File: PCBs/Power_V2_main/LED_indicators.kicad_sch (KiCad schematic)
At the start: 3 parts, among them J1 Conn_01x04, Q2 RQ6E080AJ, Q3 RQ6E080AJ

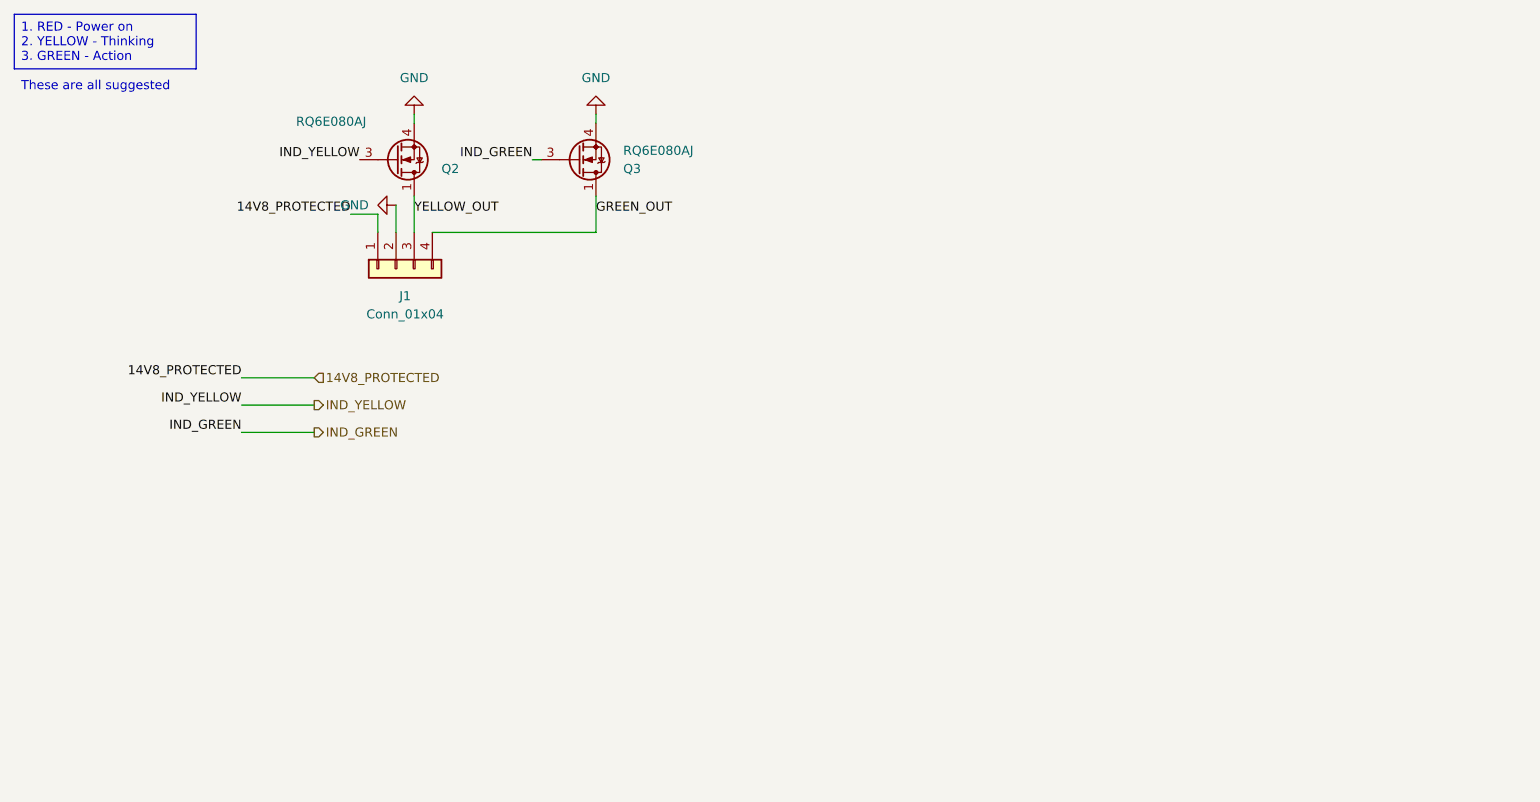
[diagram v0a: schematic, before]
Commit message: modification to LED switches
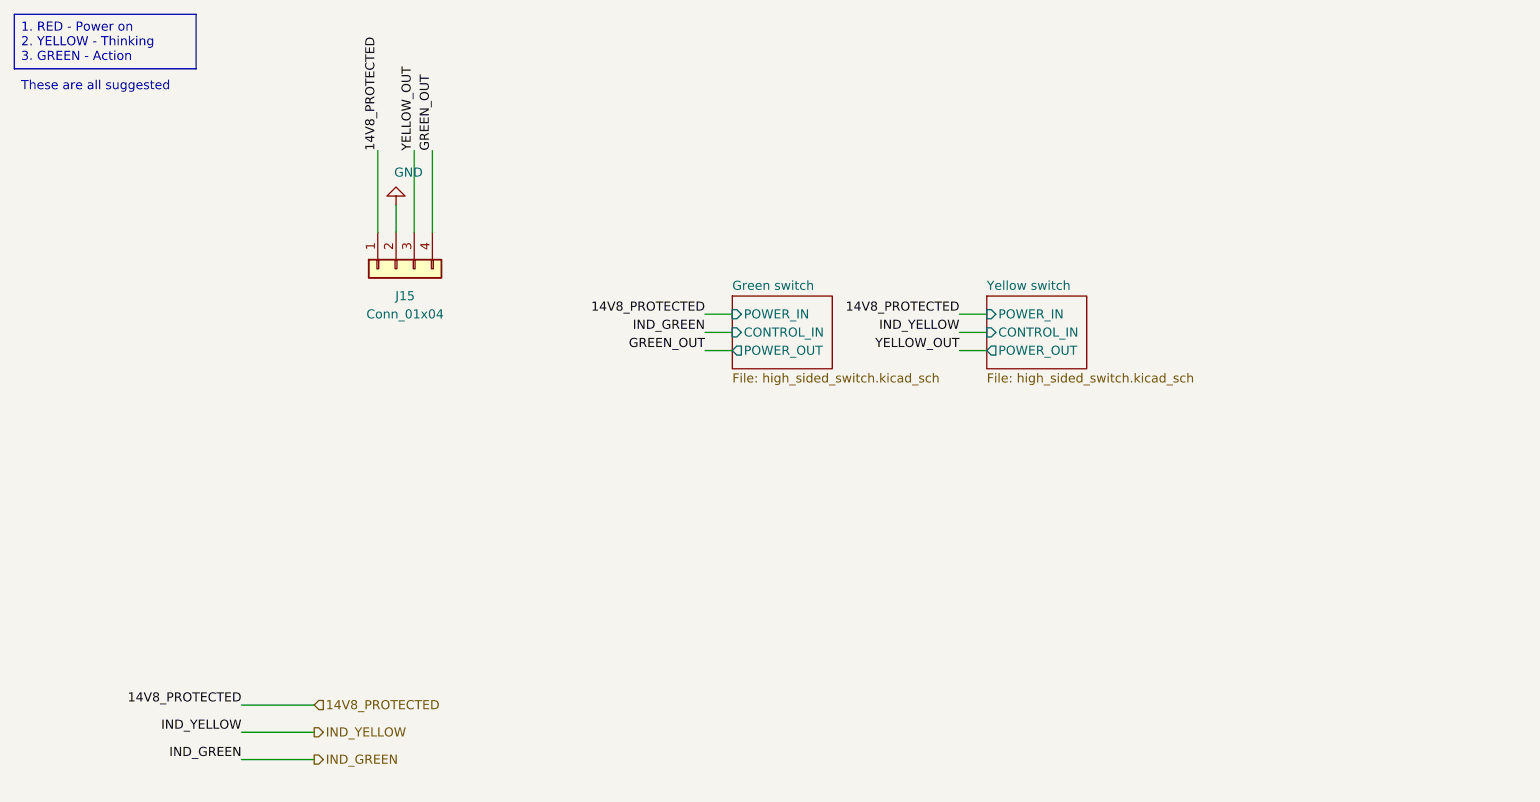
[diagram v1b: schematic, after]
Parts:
- removed J1: Conn_01x04, Connector_JST:JST_GH_BM04B-GHS-TBT_1x04-1MP_P1.25mm_Vertical, symbol Connector_Generic:Conn_01x04
- removed Q2, Q3: RQ6E080AJ, Package_TO_SOT_SMD:TSOT-23-6, symbol Transistor_FET:RQ6E080AJ
- added J15: Conn_01x04, Connector_JST:JST_GH_BM04B-GHS-TBT_1x04-1MP_P1.25mm_Vertical, symbol Connector_Generic:Conn_01x04
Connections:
- net 14V8_PROTECTED: now also J15.1 (Pin_1)
- net GND: now also J15.2 (Pin_2)
- net GREEN_OUT: now also J15.4 (Pin_4)
- net YELLOW_OUT: now also J15.3 (Pin_3)
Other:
- added sheet Green switch (high_sided_switch.kicad_sch)
- added sheet Yellow switch (high_sided_switch.kicad_sch)

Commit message: follow up changes from meeting
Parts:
- removed J15: Conn_01x04, Connector_JST:JST_GH_BM04B-GHS-TBT_1x04-1MP_P1.25mm_Vertical, symbol Connector_Generic:Conn_01x04
- added J1: Conn_01x05, Connector_JST:JST_EH_B5B-EH-A_1x05_P2.50mm_Vertical, symbol Connector_Generic:Conn_01x05
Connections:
- net 14V8_PROTECTED: now also J1.1 (Pin_1)
- net GND: now also J1.2 (Pin_2)
- net GREEN_OUT: now also J1.5 (Pin_5)
- net YELLOW_OUT: now also J1.4 (Pin_4)
- new net SIREN_OUT: J1.3 (Pin_3)
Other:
- added sheet Siren switch (high_sided_switch.kicad_sch)
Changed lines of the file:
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@@
 	(generator_version "9.0")
 	(paper "A4")
-	(text_box "1. RED - Power on\n2. YELLOW - Thinking\n3. GREEN - Action\n\nThese are all suggested"
+	(text_box "1. RED - Power on\n2. YELLOW - Thinking\n3. GREEN - Action\n4. SIREN  - All hell broken loose\n\nThese are all suggested"
 		(exclude_from_sim no)
 		(at 13.97 13.97 0)
-		(size 25.4 7.62)
+		(size 25.4 11.43)
 		(margins 0.9525 0.9525 0.9525 0.9525)
 		(stroke
@@
 	(wire
 		(pts
+			(xy 45.72 110.49) (xy 55.88 110.49)
+		)
+		(stroke
+			(width 0)
+			(type default)
+		)
+	)
+	(wire
+		(pts
+			(xy 181.61 55.88) (xy 185.42 55.88)
+		)
+		(stroke
+			(width 0)
+			(type default)
+		)
+	)
+	(wire
+		(pts
 			(xy 72.39 33.02) (xy 72.39 44.45)
 		)
@@
 	(wire
 		(pts
-			(xy 45.72 110.49) (xy 55.88 110.49)
-		)
-		(stroke
-			(width 0)
-			(type default)
-		)
-	)
-	(wire
-		(pts
 			(xy 64.77 33.02) (xy 64.77 44.45)
 		)
@@
 	(wire
 		(pts
+			(xy 181.61 60.96) (xy 185.42 60.96)
+		)
+		(stroke
+			(width 0)
+			(type default)
+		)
+	)
+	(wire
+		(pts
 			(xy 114.3 58.42) (xy 110.49 58.42)
 		)
@@
 	(wire
 		(pts
+			(xy 45.72 120.65) (xy 55.88 120.65)
+		)
+		(stroke
+			(width 0)
+			(type default)
+		)
+	)
+	(wire
+		(pts
 			(xy 110.49 60.96) (xy 114.3 60.96)
 		)
@@
 	(wire
 		(pts
+			(xy 74.93 33.02) (xy 74.93 44.45)
+		)
+		(stroke
+			(width 0)
+			(type default)
+		)
+	)
+	(wire
+		(pts
+			(xy 181.61 58.42) (xy 185.42 58.42)
+		)
+		(stroke
+			(width 0)
+			(type default)
+		)
+	)
+	(wire
+		(pts
 			(xy 69.85 33.02) (xy 69.85 44.45)
 		)
@@
 			(width 0)
 			(type default)
+		)
+	)
+	(label "IND_SIREN"
+		(at 181.61 58.42 180)
+		(effects
+			(font
+				(size 1.27 1.27)
+			)
+			(justify right bottom)
 		)
 	)
@@
 		)
 	)
-	(label "GREEN_OUT"
-		(at 72.39 33.02 90)
+	(label "SIREN_OUT"
+		(at 69.85 33.02 90)
 		(effects
 			(font
@@
 	)
 	(label "14V8_PROTECTED"
+		(at 181.61 55.88 180)
+		(effects
+			(font
+				(size 1.27 1.27)
+			)
+			(justify right bottom)
+		)
+	)
+	(label "GREEN_OUT"
+		(at 74.93 33.02 90)
+		(effects
+			(font
+				(size 1.27 1.27)
+			)
+			(justify left bottom)
+		)
+	)
+	(label "14V8_PROTECTED"
 		(at 146.05 55.88 180)
 		(effects
@@
 	)
 	(label "YELLOW_OUT"
+		(at 72.39 33.02 90)
+		(effects
+			(font
+				(size 1.27 1.27)
+			)
+			(justify left bottom)
+		)
+	)
+	(label "YELLOW_OUT"
 		(at 146.05 60.96 180)
 		(effects
@@
 			)
 			(justify right bottom)
-		)
-	)
-	(label "YELLOW_OUT"
-		(at 69.85 33.02 90)
-		(effects
-			(font
-				(size 1.27 1.27)
-			)
-			(justify left bottom)
 		)
 	)
 	(label "14V8_PROTECTED"
 		(at 45.72 110.49 180)
+		(effects
+			(font
+				(size 1.27 1.27)
+			)
+			(justify right bottom)
+		)
+	)
+	(label "IND_SIREN"
+		(at 45.72 120.65 180)
+		(effects
+			(font
+				(size 1.27 1.27)
+			)
+			(justify right bottom)
+		)
+	)
+	(label "SIREN_OUT"
+		(at 181.61 60.96 180)
 		(effects
 			(font
@@
 		(shape output)
 		(at 55.88 118.11 0)
+		(effects
+			(font
+				(size 1.27 1.27)
+			)
+			(justify left)
+		)
+	)
+	(hierarchical_label "IND_SIREN"
+		(shape output)
+		(at 55.88 120.65 0)
 		(effects
 			(font
@@
 	)
 	(symbol
-		(lib_id "Connector_Generic:Conn_01x04")
-		(at 67.31 49.53 90)
+		(lib_id "Connector_Generic:Conn_01x05")
+		(at 69.85 49.53 90)
 		(mirror x)
 		(unit 1)
@@
 		(on_board yes)
 		(dnp no)
-		(property "Reference" "J15"
-			(at 68.58 53.34 90)
-			(effects
-				(font
-					(size 1.27 1.27)
-				)
-			)
-		)
-		(property "Value" "Conn_01x04"
-			(at 68.58 55.88 90)
-			(effects
-				(font
-					(size 1.27 1.27)
-				)
-			)
-		)
-		(property "Footprint" "Connector_JST:JST_GH_BM04B-GHS-TBT_1x04-1MP_P1.25mm_Vertical"
-			(at 67.31 49.53 0)
+		(fields_autoplaced yes)
+		(property "Reference" "J1"
+			(at 69.85 53.34 90)
+			(effects
+				(font
+					(size 1.27 1.27)
+				)
+			)
+		)
+		(property "Value" "Conn_01x05"
+			(at 69.85 55.88 90)
+			(effects
+				(font
+					(size 1.27 1.27)
+				)
+			)
+		)
+		(property "Footprint" "Connector_JST:JST_EH_B5B-EH-A_1x05_P2.50mm_Vertical"
+			(at 69.85 49.53 0)
 			(effects
 				(font
@@
 		)
 		(property "Datasheet" "~"
-			(at 67.31 49.53 0)
-			(effects
-				(font
-					(size 1.27 1.27)
-				)
-				(hide yes)
-			)
-		)
-		(property "Description" "Generic connector, single row, 01x04, script generated (kicad-library-utils/schlib/autogen/connector/)"
-			(at 67.31 49.53 0)
-			(effects
-				(font
-					(size 1.27 1.27)
-				)
-				(hide yes)
-			)
+			(at 69.85 49.53 0)
+			(effects
+				(font
+					(size 1.27 1.27)
+				)
+				(hide yes)
+			)
+		)
+		(property "Description" "Generic connector, single row, 01x05, script generated (kicad-library-utils/schlib/autogen/connector/)"
+			(at 69.85 49.53 0)
+			(effects
+				(font
+					(size 1.27 1.27)
+				)
+				(hide yes)
+			)
+		)
+		(pin "2"
+		)
+		(pin "4"
+		)
+		(pin "5"
 		)
 		(pin "1"
@@
 		(pin "3"
 		)
-		(pin "4"
-		)
-		(pin "2"
+		(instances
+			(project ""
+				(path "/68375d53-ee5f-4f08-9b72-814cdcf8200e/fd663740-d58d-491a-b902-ceb831232946"
+					(reference "J1")
+					(unit 1)
+				)
+			)
+		)
+	)
+	(sheet
+		(at 185.42 53.34)
+		(size 13.97 10.16)
+		(exclude_from_sim no)
+		(in_bom yes)
+		(on_board yes)
+		(dnp no)
+		(fields_autoplaced yes)
+		(stroke
+			(width 0.1524)
+			(type solid)
+		)
+		(fill
+			(color 0 0 0 0.0000)
+		)
+		(property "Sheetname" "Siren switch"
+			(at 185.42 52.6284 0)
+			(effects
+				(font
+					(size 1.27 1.27)
+				)
+				(justify left bottom)
+			)
+		)
+		(property "Sheetfile" "high_sided_switch.kicad_sch"
+			(at 185.42 64.0846 0)
+			(effects
+				(font
+					(size 1.27 1.27)
+				)
+				(justify left top)
+			)
+		)
+		(pin "CONTROL_IN" input
+			(at 185.42 58.42 180)
+			(effects
+				(font
+					(size 1.27 1.27)
+				)
+				(justify left)
+			)
+		)
+		(pin "POWER_IN" input
+			(at 185.42 55.88 180)
+			(effects
+				(font
+					(size 1.27 1.27)
+				)
+				(justify left)
+			)
+		)
+		(pin "POWER_OUT" output
+			(at 185.42 60.96 180)
+			(effects
+				(font
+					(size 1.27 1.27)
+				)
+				(justify left)
+			)
 		)
 		(instances
 			(project "Power_V2_main"
 				(path "/68375d53-ee5f-4f08-9b72-814cdcf8200e/fd663740-d58d-491a-b902-ceb831232946"
-					(reference "J15")
-					(unit 1)
-				)
-			)
+					(page "12")
+				)
+			)

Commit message: main board ordered
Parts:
- removed J1: Conn_01x05, Connector_JST:JST_EH_B5B-EH-A_1x05_P2.50mm_Vertical, symbol Connector_Generic:Conn_01x05
- added J1, J14: Conn_01x04, Connector_JST:JST_GH_BM04B-GHS-TBT_1x04-1MP_P1.25mm_Vertical, symbol Connector_Generic:Conn_01x04
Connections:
- net 14V8_PROTECTED: now also J1.1 (Pin_1), J14.3 (Pin_3)
- net GND: now also J1.2 (Pin_2), J14.2 (Pin_2), J14.4 (Pin_4)
- net GREEN_OUT: now also J1.3 (Pin_3)
- net SIREN_OUT: now also J14.1 (Pin_1)
- net YELLOW_OUT: now also J1.4 (Pin_4)
